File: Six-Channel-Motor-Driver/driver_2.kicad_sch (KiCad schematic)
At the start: 9 parts, among them J2 Screw_Terminal_01x02, Q1 Q_NMOS_GDS, Q2 Q_NMOS_GDS, Q3 Q_NMOS_GDS, Q4 Q_NMOS_GDS

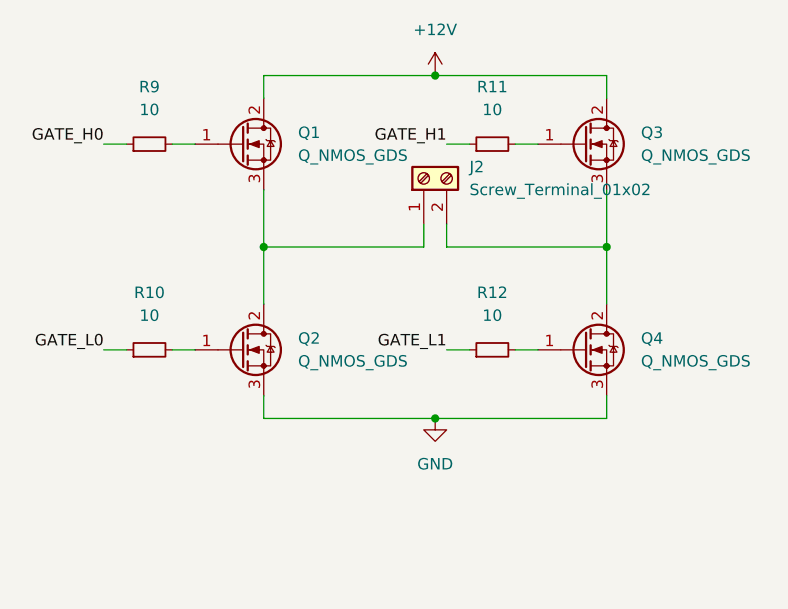
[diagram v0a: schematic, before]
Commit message: Added start of driver blocks
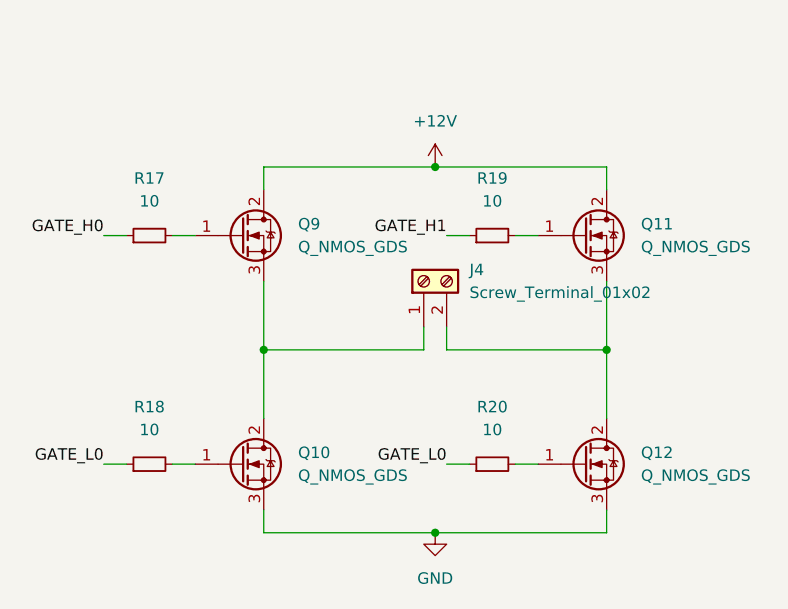
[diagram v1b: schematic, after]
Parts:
- removed J2: Screw_Terminal_01x02, Connector_Wire:SolderWire-2.5sqmm_1x02_P8.8mm_D2.4mm_OD4.4mm, symbol Connector:Screw_Terminal_01x02
- removed Q1, Q2, Q3, Q4: Q_NMOS_GDS, Package_TO_SOT_SMD:SOT-23, symbol Device:Q_NMOS_GDS
- removed R10, R11, R12, R9: 10, Resistor_SMD:R_0603_1608Metric, symbol Device:R_Small
- added J4: Screw_Terminal_01x02, Connector_Wire:SolderWire-2.5sqmm_1x02_P8.8mm_D2.4mm_OD4.4mm, symbol Connector:Screw_Terminal_01x02
- added Q10, Q11, Q12, Q9: Q_NMOS_GDS, Package_TO_SOT_SMD:SOT-23, symbol Device:Q_NMOS_GDS
- added R17, R18, R19, R20: 10, Resistor_SMD:R_0603_1608Metric, symbol Device:R_Small
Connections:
- net +12V: now also Q11.2 (D), Q9.2 (D)
- net GATE_H0: now also R17.1
- net GATE_H1: now also R19.1
- net GATE_L0: now also R18.1, R20.1
- net GND: now also Q10.3 (S), Q12.3 (S)
- new net: Q10.1 (G), R18.2
- new net: J4.1 (Pin_1), Q10.2 (D), Q9.3 (S)
- new net: Q9.1 (G), R17.2
- new net: Q12.1 (G), R20.2
- new net: J4.2 (Pin_2), Q11.3 (S), Q12.2 (D)
- new net: Q11.1 (G), R19.2
